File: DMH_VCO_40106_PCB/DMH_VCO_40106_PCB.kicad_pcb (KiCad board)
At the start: 2 copper layers, 98 x 135 mm, 144 parts, among them J10 Panel_GND, J100 IDC_02x08, J150 Conn_01x12, J300 AVR-ISP-6, Q1 BC558, Q2 BC548, Q3 BC548, Q4 BC548, Q5 BC548, Q6 BC548, Q7 J113, SW1 SW_SPDT_321_OnOff, SW2 SW_SPDT_321_OnOff, SW3 SW_SPDT_321_OnOff, U1 40106, U2 TL074, U3 TL074, U4 TL074, U5 ATtiny4313-P, U6 SM420561N

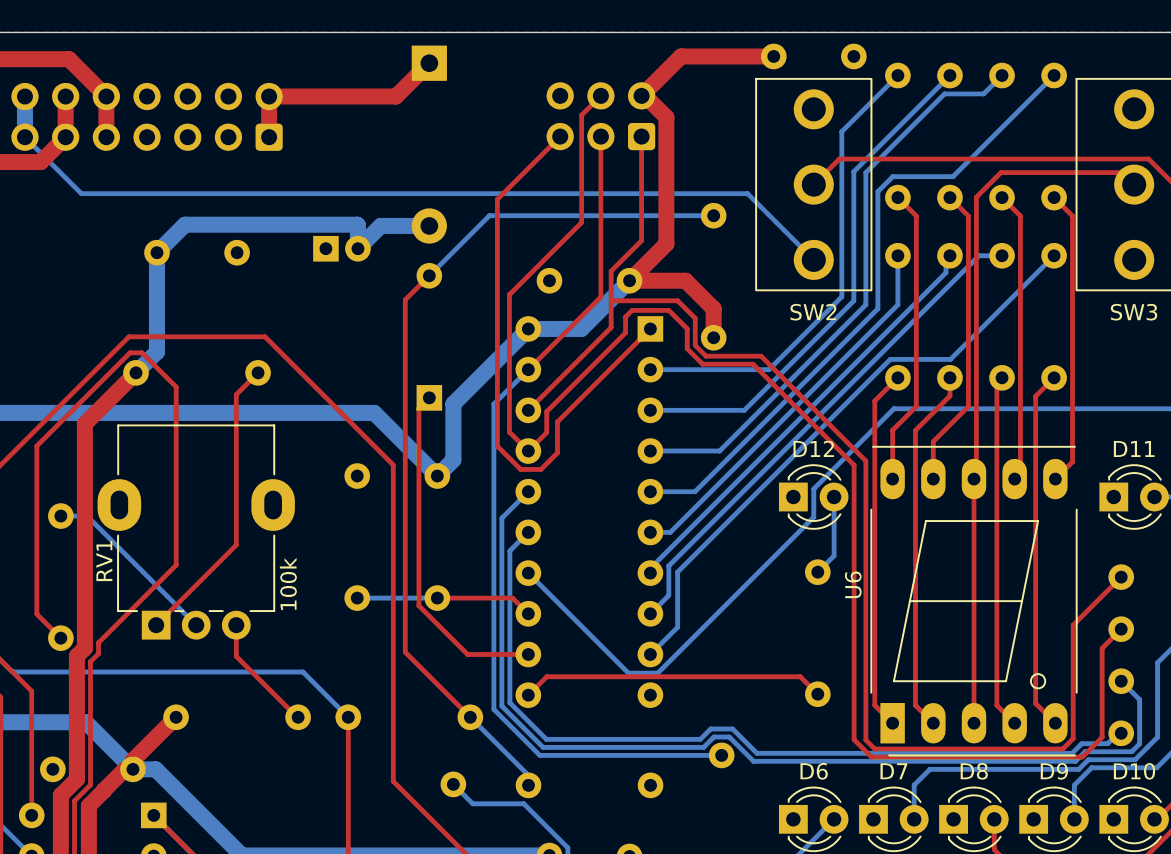
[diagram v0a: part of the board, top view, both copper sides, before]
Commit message: Removed the flat sign LED
and rerouted segments A and B to PORTD 6 and 7 respective,
and rerouted the DP segment to PORTA0
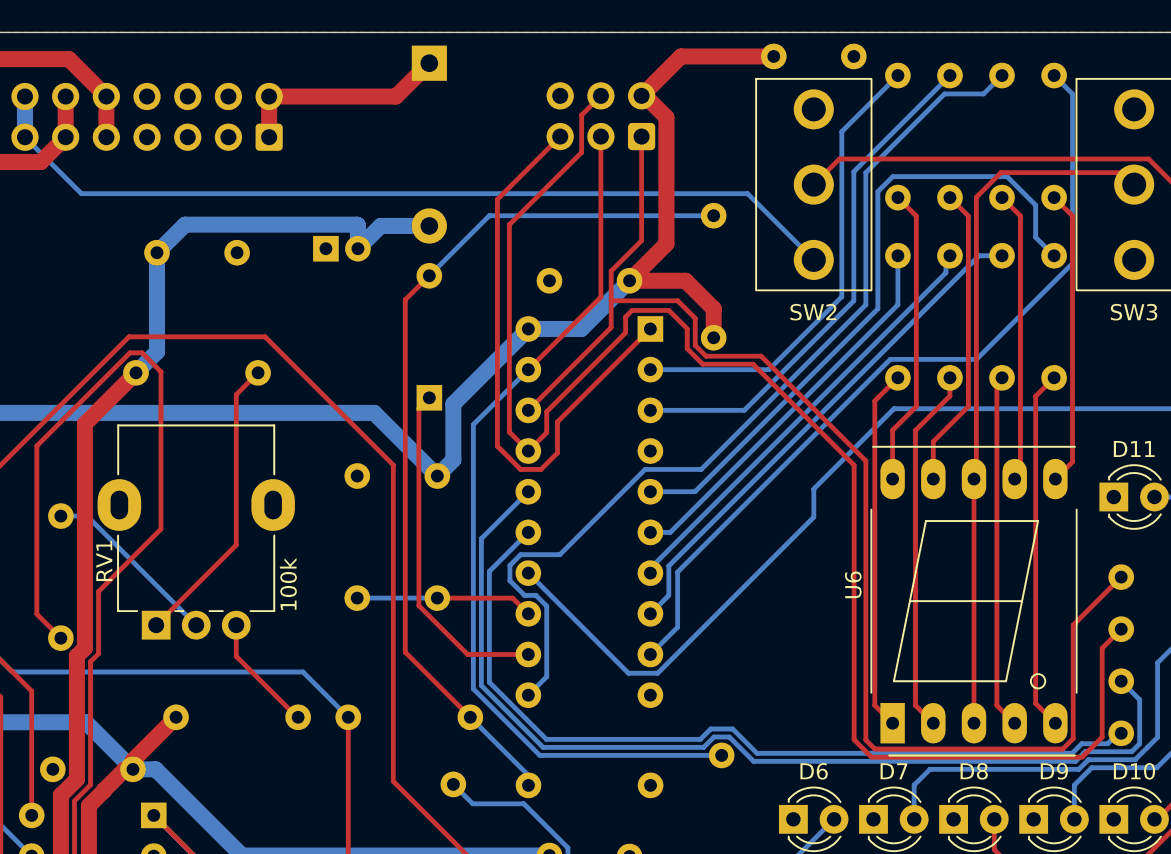
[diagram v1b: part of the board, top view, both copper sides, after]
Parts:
- removed D12: LED, LED_THT:LED_D3.0mm
- removed R74: 1k, Resistor_THT:R_Axial_DIN0207_L6.3mm_D2.5mm_P7.62mm_Horizontal
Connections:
- R60 pad 1: Net-(U5-PA1/XTAL2) -> Net-(U5-PD6)
- R61 pad 1: Net-(U5-PA0/XTAL1) -> Net-(U5-PD5)
- R67 pad 1: Net-(U5-PD5) -> Net-(U5-PA0/XTAL1)
- U5 pad 4: Net-(U5-PA1/XTAL2) -> unconnected-(U5-PA1/XTAL2-Pad4)
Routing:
- net Net-(U5-PD6): track 19.0 -> 58.2 mm
- net Net-(U5-PA1/XTAL2): track 36.5 -> 0.00 mm
- net Net-(U5-PD5): track 37.5 -> 50.7 mm
- net Net-(D12-A): track 5.11 -> 0.00 mm
- net Net-(J300-SCK): track 53.9 -> 55.0 mm
- net Net-(U5-PB4): track 60.7 -> 61.7 mm
- net Net-(U5-PB3): track 51.6 -> 52.7 mm
- net Net-(R4-Pad2): track 76.2 -> 75.4 mm
- net Net-(U5-PA0/XTAL1): track 40.2 -> 40.9 mm

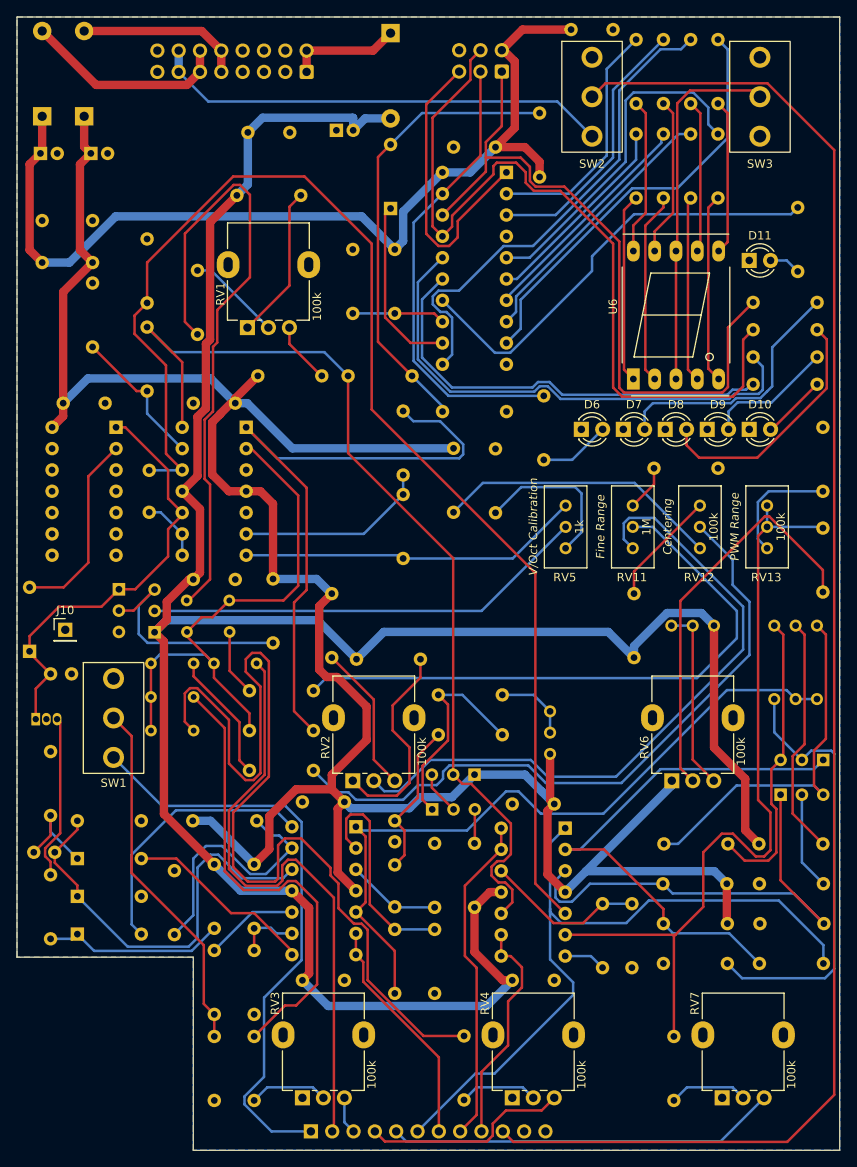
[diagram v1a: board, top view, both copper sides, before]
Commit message: Connected LEDs to Tuner On/off switch
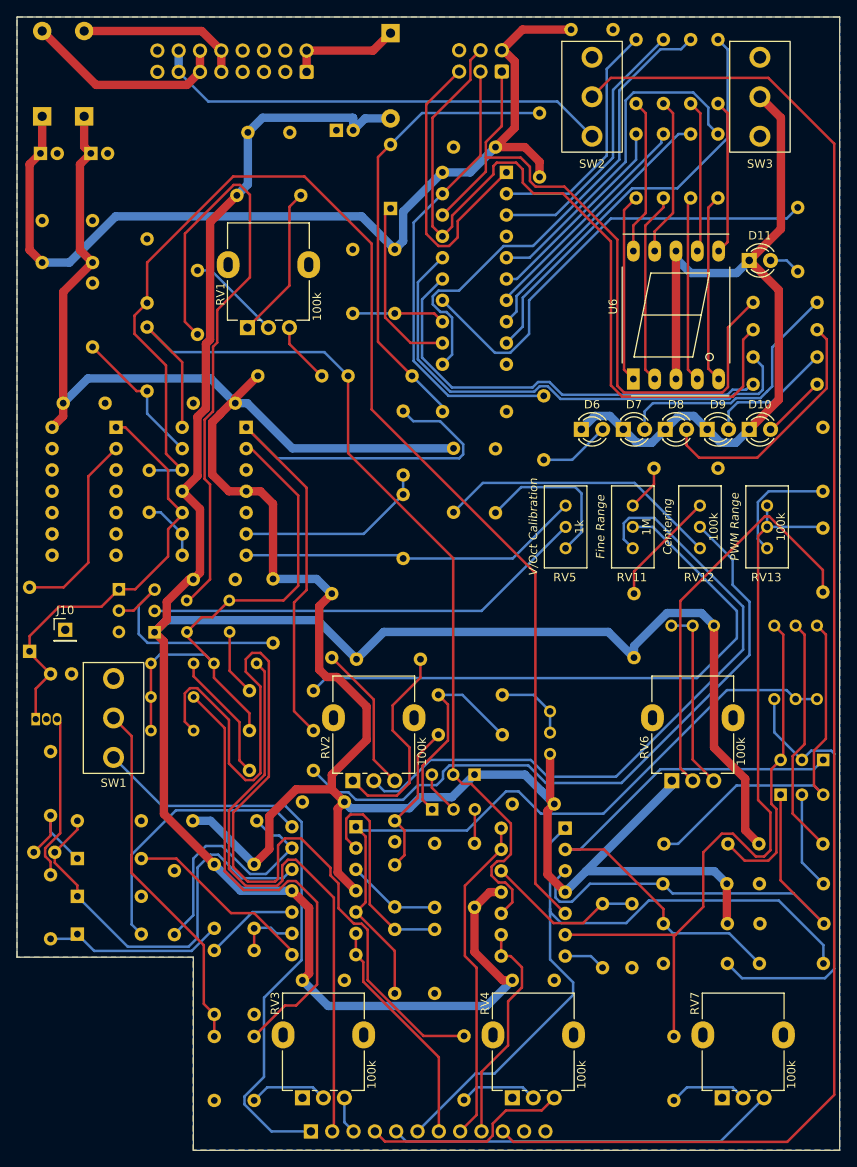
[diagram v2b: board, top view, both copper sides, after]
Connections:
- D10 pad 1: GND -> Net-(D10-K)
- D11 pad 1: GND -> Net-(D10-K)
- D6 pad 1: GND -> Net-(D10-K)
- D7 pad 1: GND -> Net-(D10-K)
- D8 pad 1: GND -> Net-(D10-K)
- D9 pad 1: GND -> Net-(D10-K)
- SW3 pad 2: Net-(SW3-B) -> Net-(D10-K)
- U6 pad 3: Net-(SW3-B) -> Net-(D10-K)
- U6 pad 8: Net-(SW3-B) -> Net-(D10-K)
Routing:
- net Net-(D10-K): track 0.00 -> 97.9 mm
- net Net-(SW3-B): track 43.7 -> 0.00 mm
- net Net-(U5-PB2): track 53.1 -> 54.4 mm
- net Net-(J150-Pin_10): track 187.8 -> 188.8 mm

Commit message: Placed input and output resistors back in main PCB
This ensures a more clear schematic and leaves the Connectors PCB only with actual connectors.
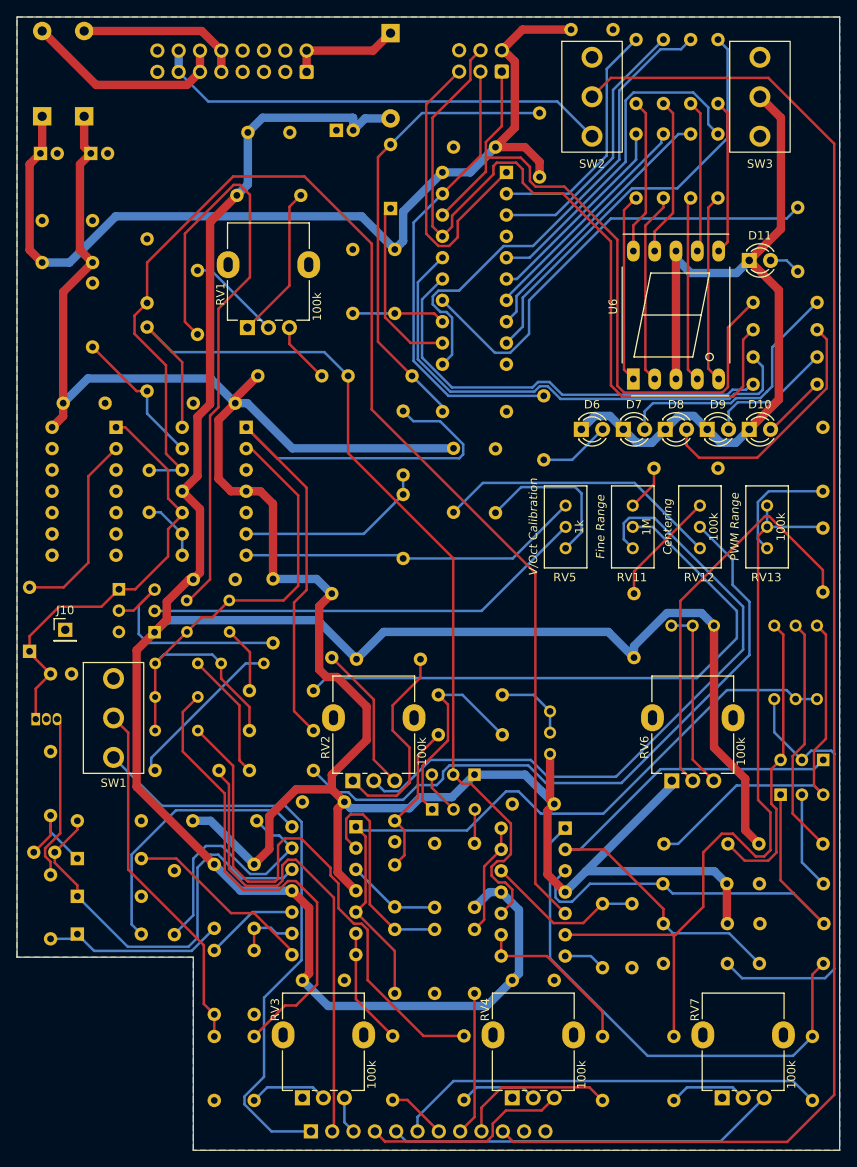
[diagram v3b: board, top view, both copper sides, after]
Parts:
- added R20: 1k, Resistor_THT:R_Axial_DIN0207_L6.3mm_D2.5mm_P7.62mm_Horizontal, B.Cu at (120.8, 183.9)
- added R21: 1k, Resistor_THT:R_Axial_DIN0207_L6.3mm_D2.5mm_P7.62mm_Horizontal, B.Cu at (105.5, 171.2)
- added R28: 1k, Resistor_THT:R_Axial_DIN0207_L6.3mm_D2.5mm_P7.62mm_Horizontal, B.Cu at (95.8, 191.5)
- added R44: 1k, Resistor_THT:R_Axial_DIN0207_L6.3mm_D2.5mm_P7.62mm_Horizontal, B.Cu at (145.8, 191.6)
- added R7: 100k, Resistor_THT:R_Axial_DIN0207_L6.3mm_D2.5mm_P7.62mm_Horizontal, B.Cu at (67.4, 152.2)
- moved TH4 0.86 mm to (80.4, 139.5)
- moved TH3 0.50 mm to (72.5, 139.5)
- moved TH5 0.50 mm to (72.5, 143.5)
- moved TH6 0.50 mm to (72.5, 147.5)
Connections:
- R36 pad 2: /Inpus and Outputs/Sine Out Jack -> Net-(R36-Pad2)
- TH4 pad 1: /Core/V/Oct In -> Net-(R7-Pad1)
- U3 pad 6: /Inpus and Outputs/Triangle Out Jack -> Net-(U3B--)
- U3 pad 7: /Inpus and Outputs/Triangle Out Jack -> Net-(U3B--)
- U4 pad 1: /Inpus and Outputs/Sine Out Jack -> Net-(R36-Pad2)
- U4 pad 13: /Core/Square Out -> Net-(U4D--)
- U4 pad 14: /Core/Square Out -> Net-(U4D--)
- U4 pad 8: /Core/Sawtooth Out -> Net-(U4C--)
- U4 pad 9: /Core/Sawtooth Out -> Net-(U4C--)
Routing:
- net Net-(R36-Pad2): track 0.00 -> 62.5 mm
- net Net-(R9-Pad2): track 114.3 -> 66.2 mm
- net /Inpus and Outputs/Sine Out Jack: track 86.0 -> 51.5 mm
- net /Core/Square Out: track 39.3 -> 17.1 mm
- net /Inpus and Outputs/Triangle Out Jack: track 27.7 -> 7.05 mm
- net Net-(U4C--): track 0.00 -> 20.3 mm
- net Net-(R7-Pad1): track 0.00 -> 19.6 mm
- net /Core/V/Oct In: track 72.1 -> 58.0 mm
- net Net-(U3B--): track 0.00 -> 14.0 mm
- net Net-(U4D--): track 0.00 -> 13.4 mm
- net /Core/Sawtooth Out: track 27.1 -> 18.9 mm
- net -12V: track 285.3 -> 287.5 mm
- net Net-(R8-Pad2): track 55.6 -> 56.8 mm
- net +12V: track 285.7 -> 284.6 mm
- net Net-(U2A--): track 66.0 -> 66.9 mm
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
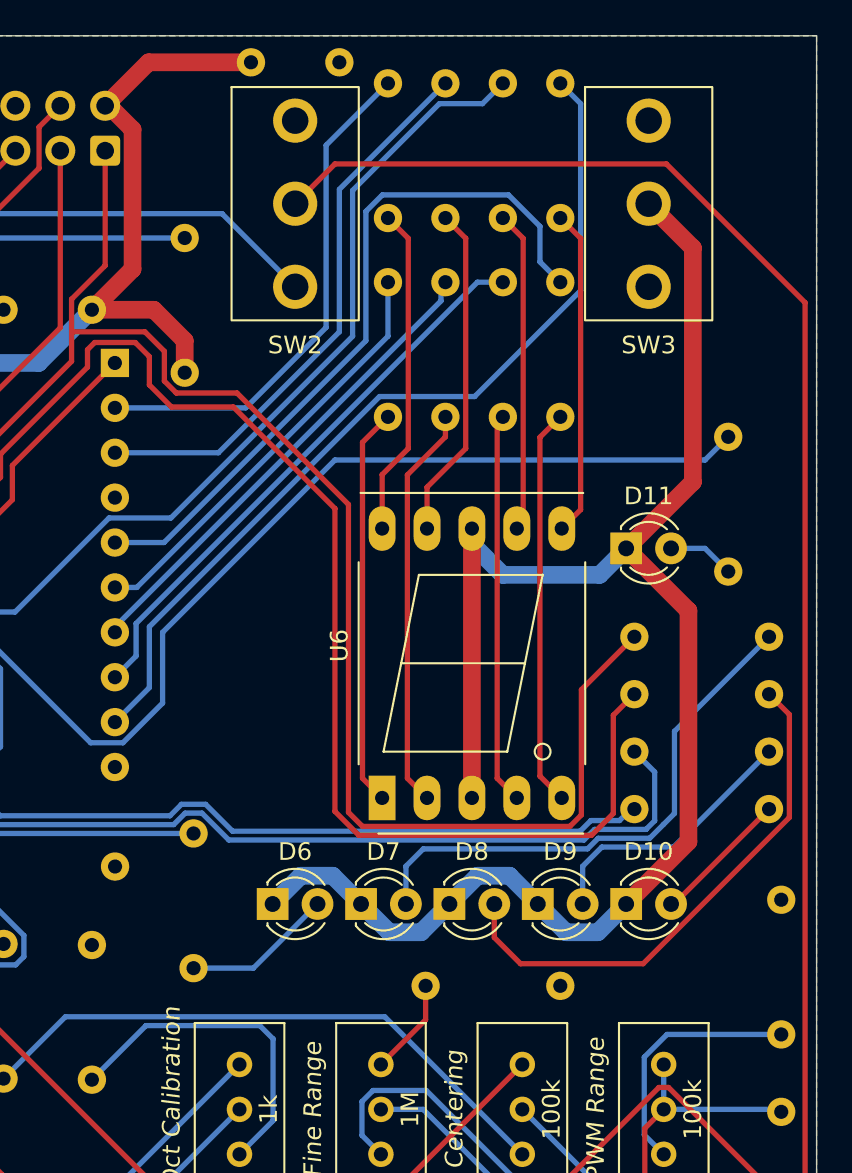
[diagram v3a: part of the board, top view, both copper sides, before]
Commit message: Connected tuner switch to uC GPIO pin
... and all LED and display segments directly to GND
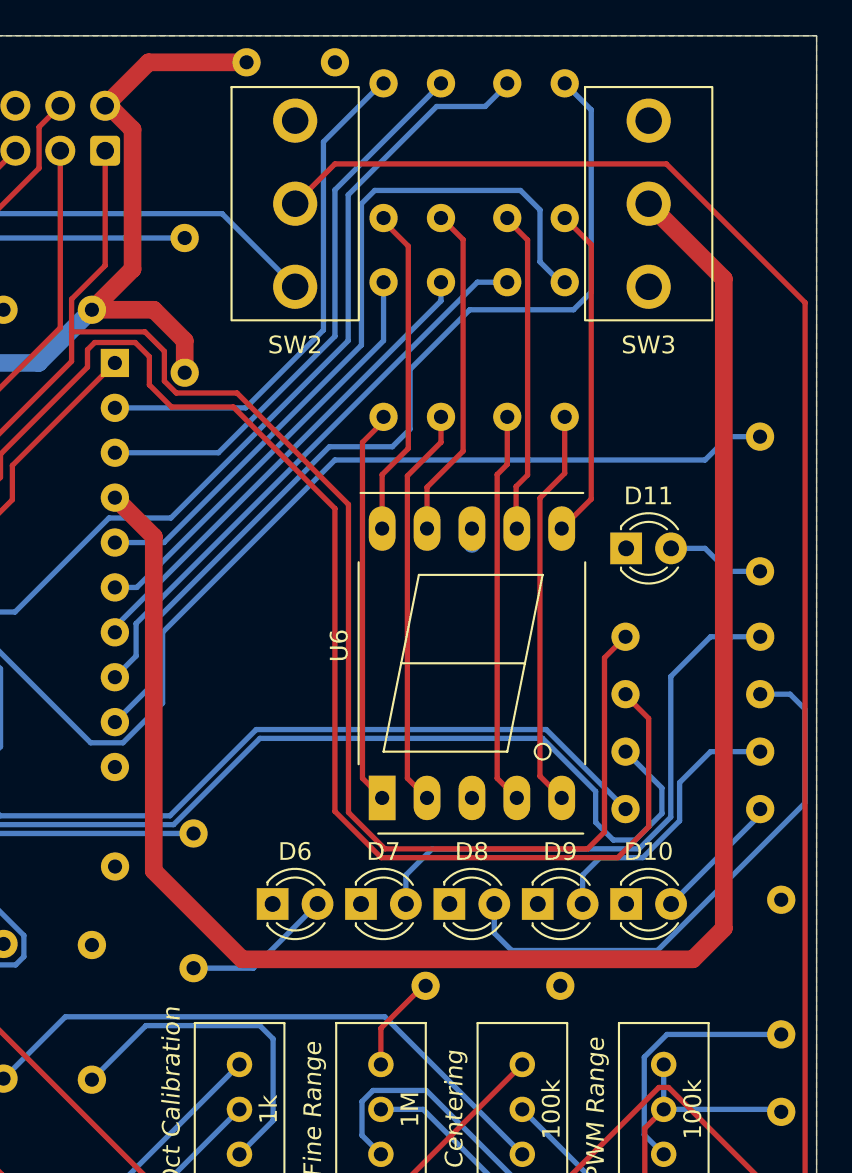
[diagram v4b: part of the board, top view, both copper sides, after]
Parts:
- moved R73 1.80 mm to (145.8, 85.2)
- moved R69 0.50 mm to (138.2, 96.5)
- moved R70 0.50 mm to (138.2, 99.8)
- moved R71 0.50 mm to (138.2, 103.0)
- moved R72 0.50 mm to (138.2, 106.2)
- moved C19 0.25 mm to (116.8, 64.0)
- moved R60 0.25 mm to (131.5, 65.2)
- moved R61 0.25 mm to (134.8, 65.2)
- moved R62 0.25 mm to (131.5, 76.4)
- moved R63 0.25 mm to (127.8, 76.4)
- moved R64 0.25 mm to (124.5, 76.4)
- moved R65 0.25 mm to (127.8, 65.2)
- moved R66 0.25 mm to (124.5, 65.2)
- moved R67 0.25 mm to (134.8, 76.4)
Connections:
- D10 pad 1: Net-(D10-K) -> GND
- D11 pad 1: Net-(D10-K) -> GND
- D6 pad 1: Net-(D10-K) -> GND
- D7 pad 1: Net-(D10-K) -> GND
- D8 pad 1: Net-(D10-K) -> GND
- D9 pad 1: Net-(D10-K) -> GND
- SW3 pad 1: GND -> unconnected-(SW3-C-Pad1)
- SW3 pad 2: Net-(D10-K) -> Net-(SW3-B)
- SW3 pad 3: unconnected-(SW3-A-Pad3) -> GND
- U5 pad 4: unconnected-(U5-PA1/XTAL2-Pad4) -> Net-(SW3-B)
- U6 pad 3: Net-(D10-K) -> GND
- U6 pad 8: Net-(D10-K) -> GND
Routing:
- net Net-(SW3-B): track 0.00 -> 99.8 mm
- net Net-(D10-K): track 97.9 -> 0.00 mm
- net Net-(U5-PB4): track 61.7 -> 66.8 mm
- net Net-(J300-MOSI): track 96.1 -> 99.8 mm
- net Net-(U5-PD5): track 50.7 -> 53.5 mm
- net Net-(J300-MISO): track 83.2 -> 85.9 mm
- net Net-(U5-PB3): track 52.7 -> 55.2 mm
- net Net-(D11-A): track 3.78 -> 5.58 mm
- net Net-(U5-PB2): track 54.4 -> 56.2 mm
- net Net-(D7-A): track 30.8 -> 32.4 mm
- net Net-(D9-A): track 15.4 -> 17.0 mm
- net Net-(U5-PA0/XTAL1): track 40.9 -> 42.0 mm
- net GND: track 0.00 -> 1.11 mm
- net Net-(D8-A): track 30.1 -> 30.8 mm
